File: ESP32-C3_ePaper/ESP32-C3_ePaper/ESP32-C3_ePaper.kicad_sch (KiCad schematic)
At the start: 0 parts

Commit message: ESP32-C3 ePaper
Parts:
- added J1: e-Paper, Alexander Footprints Library:Conn_ePaper, symbol Alexander Symbols Library:Conn_ePaper_01x08
- added U1: ESP32-C3 SuperMini, Alexander Footprint Library:ESP32-C3_SuperMini, symbol Alexander Symbols Library:ESP32-C3-SuperMini
- added U2: ~, symbol Alexander Symbols Library:ESP32C3_ZenBoard
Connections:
- new net GNDD: J1.GND, U1.15 (GND), U2.9 (G)

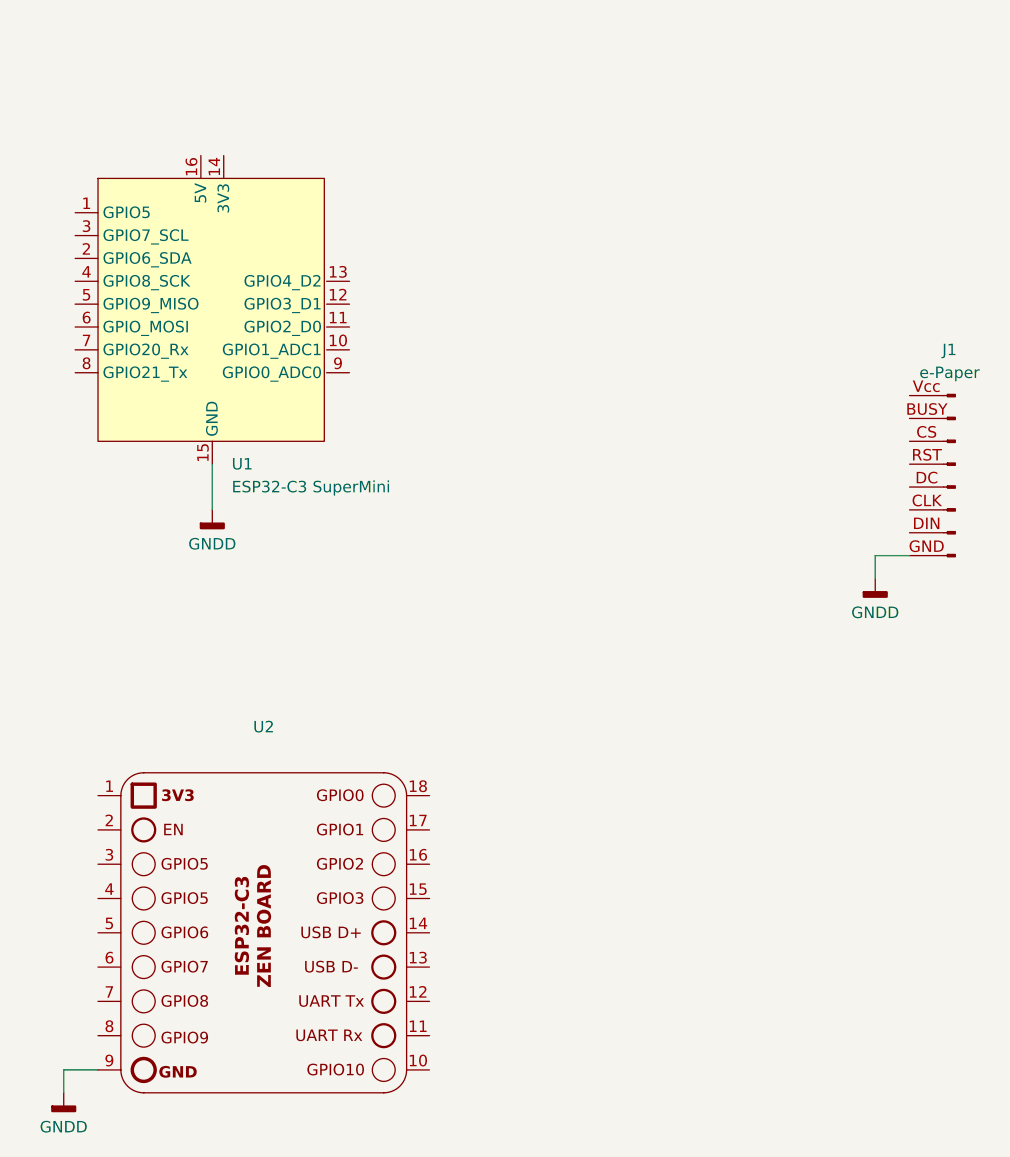
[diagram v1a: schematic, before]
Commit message: ESP32-C3 ePaper
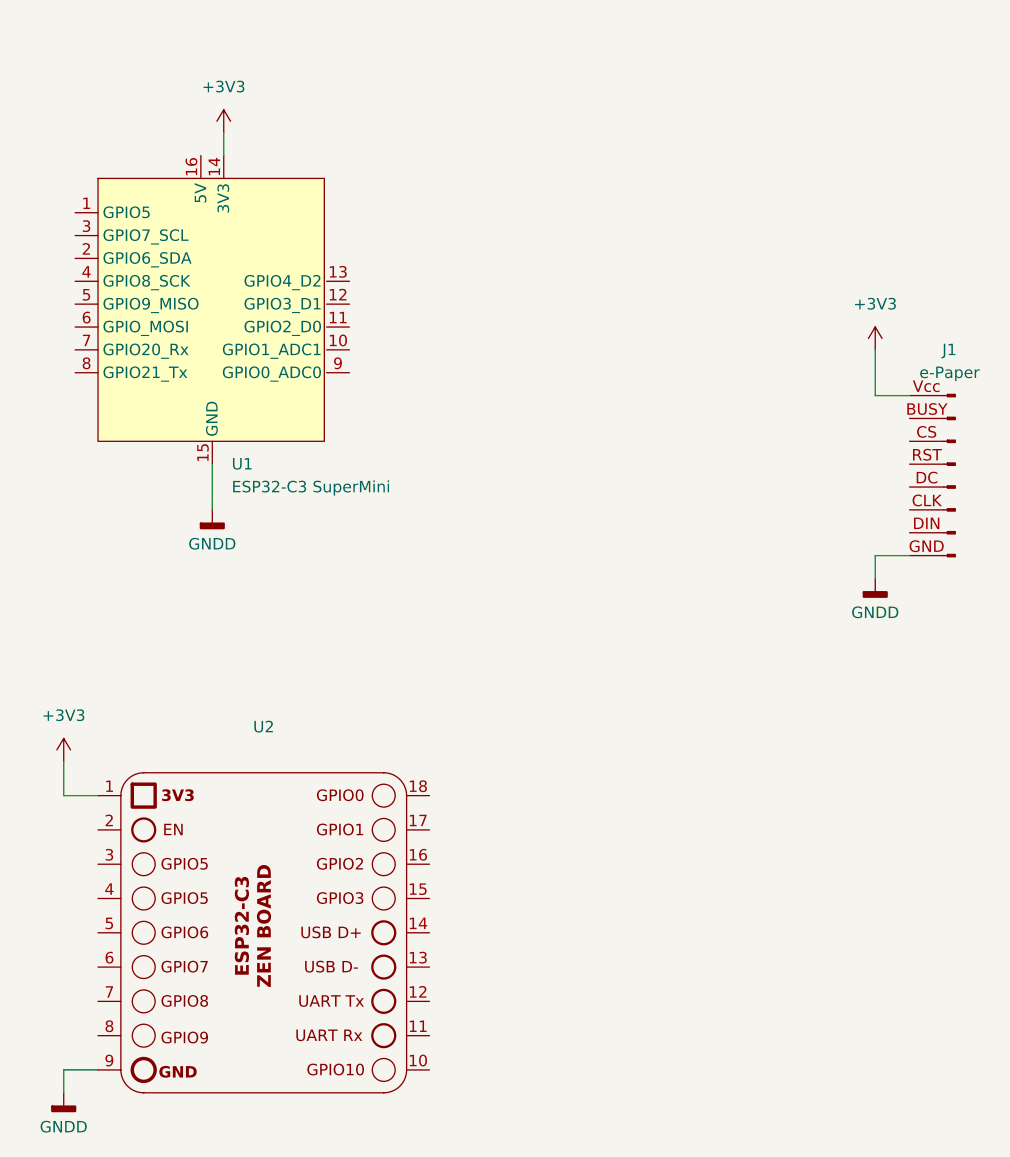
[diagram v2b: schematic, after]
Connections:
- net +3V3: now reaches J1.Vcc
- net +3V3: now also U1.14 (3V3), U2.1 (3V3)
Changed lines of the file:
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@@
+	(wire
+		(pts
+			(xy 156.21 67.31) (xy 152.4 67.31)
+		)
+		(stroke
+			(width 0)
+			(type default)
+		)
+	)
+	(wire
+		(pts
+			(xy 152.4 67.31) (xy 152.4 62.23)
+		)
+		(stroke
+			(width 0)
+			(type default)
+		)
+	)
 	(wire
 		(pts
@@
 	(wire
 		(pts
+			(xy 66.04 111.76) (xy 62.23 111.76)
+		)
+		(stroke
+			(width 0)
+			(type default)
+		)
+	)
+	(wire
+		(pts
 			(xy 152.4 87.63) (xy 152.4 85.09)
+		)
+		(stroke
+			(width 0)
+			(type default)
+		)
+	)
+	(wire
+		(pts
+			(xy 80.01 38.1) (xy 80.01 40.64)
+		)
+		(stroke
+			(width 0)
+			(type default)
+		)
+	)
+	(wire
+		(pts
+			(xy 62.23 111.76) (xy 62.23 107.95)
 		)
 		(stroke
@@
 	)
 	(symbol
+		(lib_id "power:+3V3")
+		(at 152.4 62.23 0)
+		(unit 1)
+		(exclude_from_sim no)
+		(in_bom yes)
+		(on_board yes)
+		(dnp no)
+		(fields_autoplaced yes)
+		(property "Reference" "#PWR04"
+			(at 152.4 66.04 0)
+			(effects
+				(font
+					(size 1.27 1.27)
+				)
+				(hide yes)
+			)
+		)
+		(property "Value" "+3V3"
+			(at 152.4 57.15 0)
+			(effects
+				(font
+					(size 1.27 1.27)
+				)
+			)
+		)
+		(property "Footprint" ""
+			(at 152.4 62.23 0)
+			(effects
+				(font
+					(size 1.27 1.27)
+				)
+				(hide yes)
+			)
+		)
+		(property "Datasheet" ""
+			(at 152.4 62.23 0)
+			(effects
+				(font
+					(size 1.27 1.27)
+				)
+				(hide yes)
+			)
+		)
+		(property "Description" "Power symbol creates a global label with name \"+3V3\""
+			(at 152.4 62.23 0)
+			(effects
+				(font
+					(size 1.27 1.27)
+				)
+				(hide yes)
+			)
+		)
+		(pin "1"
+		)
+		(instances
+			(project ""
+				(path "/95feff10-2965-4a71-88b6-e41b0fca8232"
+					(reference "#PWR04")
+					(unit 1)
+				)
+			)
+		)
+	)
+	(symbol
+		(lib_id "power:+3V3")
+		(at 80.01 38.1 0)
+		(unit 1)
+		(exclude_from_sim no)
+		(in_bom yes)
+		(on_board yes)
+		(dnp no)
+		(fields_autoplaced yes)
+		(property "Reference" "#PWR05"
+			(at 80.01 41.91 0)
+			(effects
+				(font
+					(size 1.27 1.27)
+				)
+				(hide yes)
+			)
+		)
+		(property "Value" "+3V3"
+			(at 80.01 33.02 0)
+			(effects
+				(font
+					(size 1.27 1.27)
+				)
+			)
+		)
+		(property "Footprint" ""
+			(at 80.01 38.1 0)
+			(effects
+				(font
+					(size 1.27 1.27)
+				)
+				(hide yes)
+			)
+		)
+		(property "Datasheet" ""
+			(at 80.01 38.1 0)
+			(effects
+				(font
+					(size 1.27 1.27)
+				)
+				(hide yes)
+			)
+		)
+		(property "Description" "Power symbol creates a global label with name \"+3V3\""
+			(at 80.01 38.1 0)
+			(effects
+				(font
+					(size 1.27 1.27)
+				)
+				(hide yes)
+			)
+		)
+		(pin "1"
+		)
+		(instances
+			(project ""
+				(path "/95feff10-2965-4a71-88b6-e41b0fca8232"
+					(reference "#PWR05")
+					(unit 1)
+				)
+			)
+		)
+	)
+	(symbol
 		(lib_id "power:GNDD")
 		(at 152.4 87.63 0)
@@
 					(unit 1)
 				)
+			)
+		)
+	)
+	(symbol
+		(lib_id "power:+3V3")
+		(at 62.23 107.95 0)
+		(unit 1)
+		(exclude_from_sim no)
+		(in_bom yes)
+		(on_board yes)
+		(dnp no)
+		(fields_autoplaced yes)
+		(property "Reference" "#PWR06"
+			(at 62.23 111.76 0)
+			(effects
+				(font
+					(size 1.27 1.27)
+				)
+				(hide yes)
+			)
+		)
+		(property "Value" "+3V3"
+			(at 62.23 102.87 0)
+			(effects
+				(font
+					(size 1.27 1.27)
+				)
+			)
+		)
+		(property "Footprint" ""
+			(at 62.23 107.95 0)
+			(effects
+				(font
+					(size 1.27 1.27)
+				)
+				(hide yes)
+			)
+		)
+		(property "Datasheet" ""
+			(at 62.23 107.95 0)
+			(effects
+				(font
+					(size 1.27 1.27)
+				)
+				(hide yes)
+			)
+		)
+		(property "Description" "Power symbol creates a global label with name \"+3V3\""
+			(at 62.23 107.95 0)
+			(effects
+				(font
+					(size 1.27 1.27)
+				)
+				(hide yes)
+			)
+		)
+		(pin "1"
+		)
+		(instances
+			(project ""
+				(path "/95feff10-2965-4a71-88b6-e41b0fca8232"
+					(reference "#PWR06")
+					(unit 1)
+				)

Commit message: ESP32-C3 ePaper
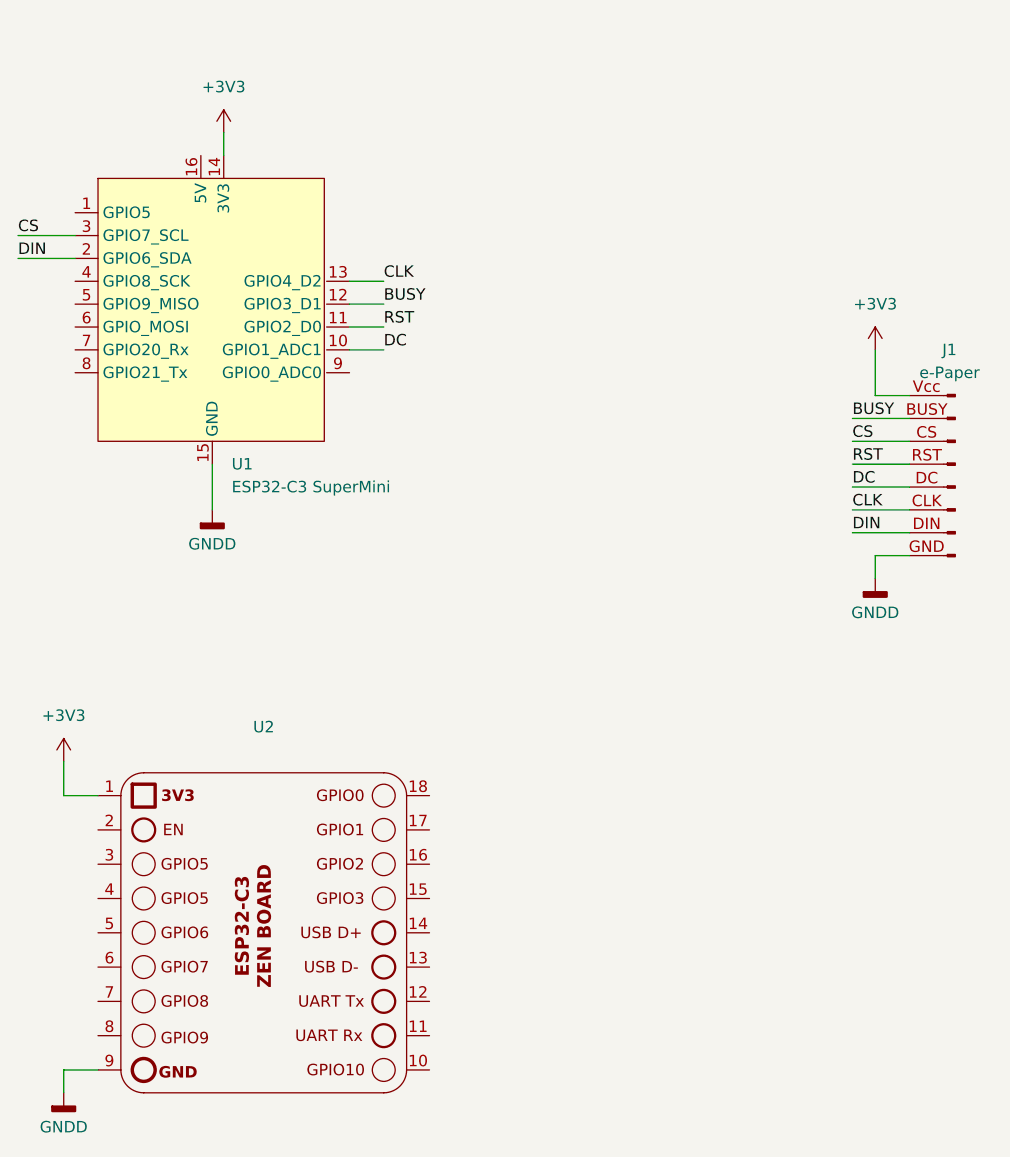
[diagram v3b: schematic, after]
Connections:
- net BUSY: now reaches J1.BUSY
- net BUSY: now also U1.12 (GPIO3_D1)
- net CLK: now reaches J1.CLK
- net CLK: now also U1.13 (GPIO4_D2)
- net CS: now reaches J1.CS
- net CS: now also U1.3 (GPIO7_SCL)
- net DC: now reaches J1.DC
- net DC: now also U1.10 (GPIO1_ADC1)
- net DIN: now reaches J1.DIN
- net DIN: now also U1.2 (GPIO6_SDA)
- net RST: now reaches J1.RST
- net RST: now also U1.11 (GPIO2_D0)
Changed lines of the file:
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@@
+	(wire
+		(pts
+			(xy 149.86 74.93) (xy 156.21 74.93)
+		)
+		(stroke
+			(width 0)
+			(type default)
+		)
+	)
+	(wire
+		(pts
+			(xy 57.15 52.07) (xy 63.5 52.07)
+		)
+		(stroke
+			(width 0)
+			(type default)
+		)
+	)
 	(wire
 		(pts
@@
 	(wire
 		(pts
+			(xy 57.15 49.53) (xy 63.5 49.53)
+		)
+		(stroke
+			(width 0)
+			(type default)
+		)
+	)
+	(wire
+		(pts
 			(xy 152.4 67.31) (xy 152.4 62.23)
 		)
@@
 	(wire
 		(pts
+			(xy 149.86 82.55) (xy 156.21 82.55)
+		)
+		(stroke
+			(width 0)
+			(type default)
+		)
+	)
+	(wire
+		(pts
 			(xy 78.74 74.93) (xy 78.74 80.01)
 		)
@@
 	(wire
 		(pts
+			(xy 149.86 69.85) (xy 156.21 69.85)
+		)
+		(stroke
+			(width 0)
+			(type default)
+		)
+	)
+	(wire
+		(pts
 			(xy 152.4 87.63) (xy 152.4 85.09)
 		)
@@
 	(wire
 		(pts
+			(xy 149.86 80.01) (xy 156.21 80.01)
+		)
+		(stroke
+			(width 0)
+			(type default)
+		)
+	)
+	(wire
+		(pts
+			(xy 149.86 77.47) (xy 156.21 77.47)
+		)
+		(stroke
+			(width 0)
+			(type default)
+		)
+	)
+	(wire
+		(pts
+			(xy 93.98 62.23) (xy 97.79 62.23)
+		)
+		(stroke
+			(width 0)
+			(type default)
+		)
+	)
+	(wire
+		(pts
 			(xy 62.23 111.76) (xy 62.23 107.95)
 		)
@@
 	(wire
 		(pts
+			(xy 93.98 57.15) (xy 97.79 57.15)
+		)
+		(stroke
+			(width 0)
+			(type default)
+		)
+	)
+	(wire
+		(pts
+			(xy 93.98 54.61) (xy 97.79 54.61)
+		)
+		(stroke
+			(width 0)
+			(type default)
+		)
+	)
+	(wire
+		(pts
 			(xy 152.4 85.09) (xy 156.21 85.09)
 		)
@@
 	(wire
 		(pts
+			(xy 93.98 59.69) (xy 97.79 59.69)
+		)
+		(stroke
+			(width 0)
+			(type default)
+		)
+	)
+	(wire
+		(pts
 			(xy 62.23 142.24) (xy 66.04 142.24)
 		)
@@
 		)
 	)
+	(wire
+		(pts
+			(xy 149.86 72.39) (xy 156.21 72.39)
+		)
+		(stroke
+			(width 0)
+			(type default)
+		)
+	)
+	(label "DIN"
+		(at 57.15 52.07 0)
+		(effects
+			(font
+				(size 1.27 1.27)
+			)
+			(justify left bottom)
+		)
+	)
+	(label "DIN"
+		(at 149.86 82.55 0)
+		(effects
+			(font
+				(size 1.27 1.27)
+			)
+			(justify left bottom)
+		)
+	)
+	(label "DC"
+		(at 97.79 62.23 0)
+		(effects
+			(font
+				(size 1.27 1.27)
+			)
+			(justify left bottom)
+		)
+	)
+	(label "BUSY"
+		(at 97.79 57.15 0)
+		(effects
+			(font
+				(size 1.27 1.27)
+			)
+			(justify left bottom)
+		)
+	)
+	(label "RST"
+		(at 149.86 74.93 0)
+		(effects
+			(font
+				(size 1.27 1.27)
+			)
+			(justify left bottom)
+		)
+	)
+	(label "CS"
+		(at 149.86 72.39 0)
+		(effects
+			(font
+				(size 1.27 1.27)
+			)
+			(justify left bottom)
+		)
+	)
+	(label "CLK"
+		(at 97.79 54.61 0)
+		(effects
+			(font
+				(size 1.27 1.27)
+			)
+			(justify left bottom)
+		)
+	)
+	(label "CS"
+		(at 57.15 49.53 0)
+		(effects
+			(font
+				(size 1.27 1.27)
+			)
+			(justify left bottom)
+		)
+	)
+	(label "RST"
+		(at 97.79 59.69 0)
+		(effects
+			(font
+				(size 1.27 1.27)
+			)
+			(justify left bottom)
+		)
+	)
+	(label "DC"
+		(at 149.86 77.47 0)
+		(effects
+			(font
+				(size 1.27 1.27)
+			)
+			(justify left bottom)
+		)
+	)
+	(label "BUSY"
+		(at 149.86 69.85 0)
+		(effects
+			(font
+				(size 1.27 1.27)
+			)
+			(justify left bottom)
+		)
+	)
+	(label "CLK"
+		(at 149.86 80.01 0)
+		(effects
+			(font
+				(size 1.27 1.27)
+			)
+			(justify left bottom)
+		)
+	)

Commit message: ESP32-C3 ePaper
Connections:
- net BUSY: now also U2.15 (GPIO3)
- net CLK: now also U2.12 (Tx)
- net CS: now also U2.6 (GPIO7)
- net DC: now also U2.17 (GPIO1)
- net DIN: now also U2.5 (GPIO6)
- net RST: now also U2.16 (GPIO2)
- net +5VD: now reaches U1.16 (5V)
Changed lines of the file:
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@@
+	(wire
+		(pts
+			(xy 102.87 123.19) (xy 106.68 123.19)
+		)
+		(stroke
+			(width 0)
+			(type default)
+		)
+	)
+	(wire
+		(pts
+			(xy 59.69 127) (xy 66.04 127)
+		)
+		(stroke
+			(width 0)
+			(type default)
+		)
+	)
+	(wire
+		(pts
+			(xy 102.87 115.57) (xy 106.68 115.57)
+		)
+		(stroke
+			(width 0)
+			(type default)
+		)
+	)
 	(wire
 		(pts
@@
 	(wire
 		(pts
+			(xy 102.87 134.62) (xy 106.68 134.62)
+		)
+		(stroke
+			(width 0)
+			(type default)
+		)
+	)
+	(wire
+		(pts
 			(xy 57.15 52.07) (xy 63.5 52.07)
 		)
@@
 	(wire
 		(pts
+			(xy 59.69 130.81) (xy 66.04 130.81)
+		)
+		(stroke
+			(width 0)
+			(type default)
+		)
+	)
+	(wire
+		(pts
 			(xy 80.01 38.1) (xy 80.01 40.64)
 		)
@@
 		(pts
 			(xy 93.98 62.23) (xy 97.79 62.23)
+		)
+		(stroke
+			(width 0)
+			(type default)
+		)
+	)
+	(wire
+		(pts
+			(xy 102.87 119.38) (xy 106.68 119.38)
+		)
+		(stroke
+			(width 0)
+			(type default)
+		)
+	)
+	(wire
+		(pts
+			(xy 77.47 31.75) (xy 77.47 40.64)
 		)
 		(stroke
@@
 		)
 	)
+	(label "RST"
+		(at 106.68 119.38 0)
+		(effects
+			(font
+				(size 1.27 1.27)
+			)
+			(justify left bottom)
+		)
+	)
+	(label "CLK"
+		(at 106.68 134.62 0)
+		(effects
+			(font
+				(size 1.27 1.27)
+			)
+			(justify left bottom)
+		)
+	)
 	(label "BUSY"
 		(at 97.79 57.15 0)
@@
 	)
 	(label "CS"
+		(at 59.69 130.81 0)
+		(effects
+			(font
+				(size 1.27 1.27)
+			)
+			(justify left bottom)
+		)
+	)
+	(label "CS"
 		(at 149.86 72.39 0)
+		(effects
+			(font
+				(size 1.27 1.27)
+			)
+			(justify left bottom)
+		)
+	)
+	(label "DC"
+		(at 106.68 115.57 0)
 		(effects
 			(font
@@
 		)
 	)
+	(label "BUSY"
+		(at 106.68 123.19 0)
+		(effects
+			(font
+				(size 1.27 1.27)
+			)
+			(justify left bottom)
+		)
+	)
 	(label "DC"
 		(at 149.86 77.47 0)
@@
 	(label "BUSY"
 		(at 149.86 69.85 0)
+		(effects
+			(font
+				(size 1.27 1.27)
+			)
+			(justify left bottom)
+		)
+	)
+	(label "DIN"
+		(at 59.69 127 0)
 		(effects
 			(font
@@
 					(unit 1)
 				)
+			)
+		)
+	)
+	(symbol
+		(lib_id "power:+5VD")
+		(at 77.47 31.75 0)
+		(unit 1)
+		(exclude_from_sim no)
+		(in_bom yes)
+		(on_board yes)
+		(dnp no)
+		(fields_autoplaced yes)
+		(property "Reference" "#PWR07"
+			(at 77.47 35.56 0)
+			(effects
+				(font
+					(size 1.27 1.27)
+				)
+				(hide yes)
+			)
+		)
+		(property "Value" "+5VD"
+			(at 77.47 26.67 0)
+			(effects
+				(font
+					(size 1.27 1.27)
+				)
+			)
+		)
+		(property "Footprint" ""
+			(at 77.47 31.75 0)
+			(effects
+				(font
+					(size 1.27 1.27)
+				)
+				(hide yes)
+			)
+		)
+		(property "Datasheet" ""
+			(at 77.47 31.75 0)
+			(effects
+				(font
+					(size 1.27 1.27)
+				)
+				(hide yes)
+			)
+		)
+		(property "Description" "Power symbol creates a global label with name \"+5VD\""
+			(at 77.47 31.75 0)
+			(effects
+				(font
+					(size 1.27 1.27)
+				)
+				(hide yes)
+			)
+		)
+		(pin "1"
+		)
+		(instances
+			(project ""
+				(path "/95feff10-2965-4a71-88b6-e41b0fca8232"
+					(reference "#PWR07")
+					(unit 1)
+				)
